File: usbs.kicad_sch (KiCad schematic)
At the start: 17 parts, among them J4 USB-A_Amphenol_UE27AC54100, J5 USB-C_GCT_USB4105-GF-A, J6 USB-C_GCT_USB4105-GF-A, U5 FT234XD-R

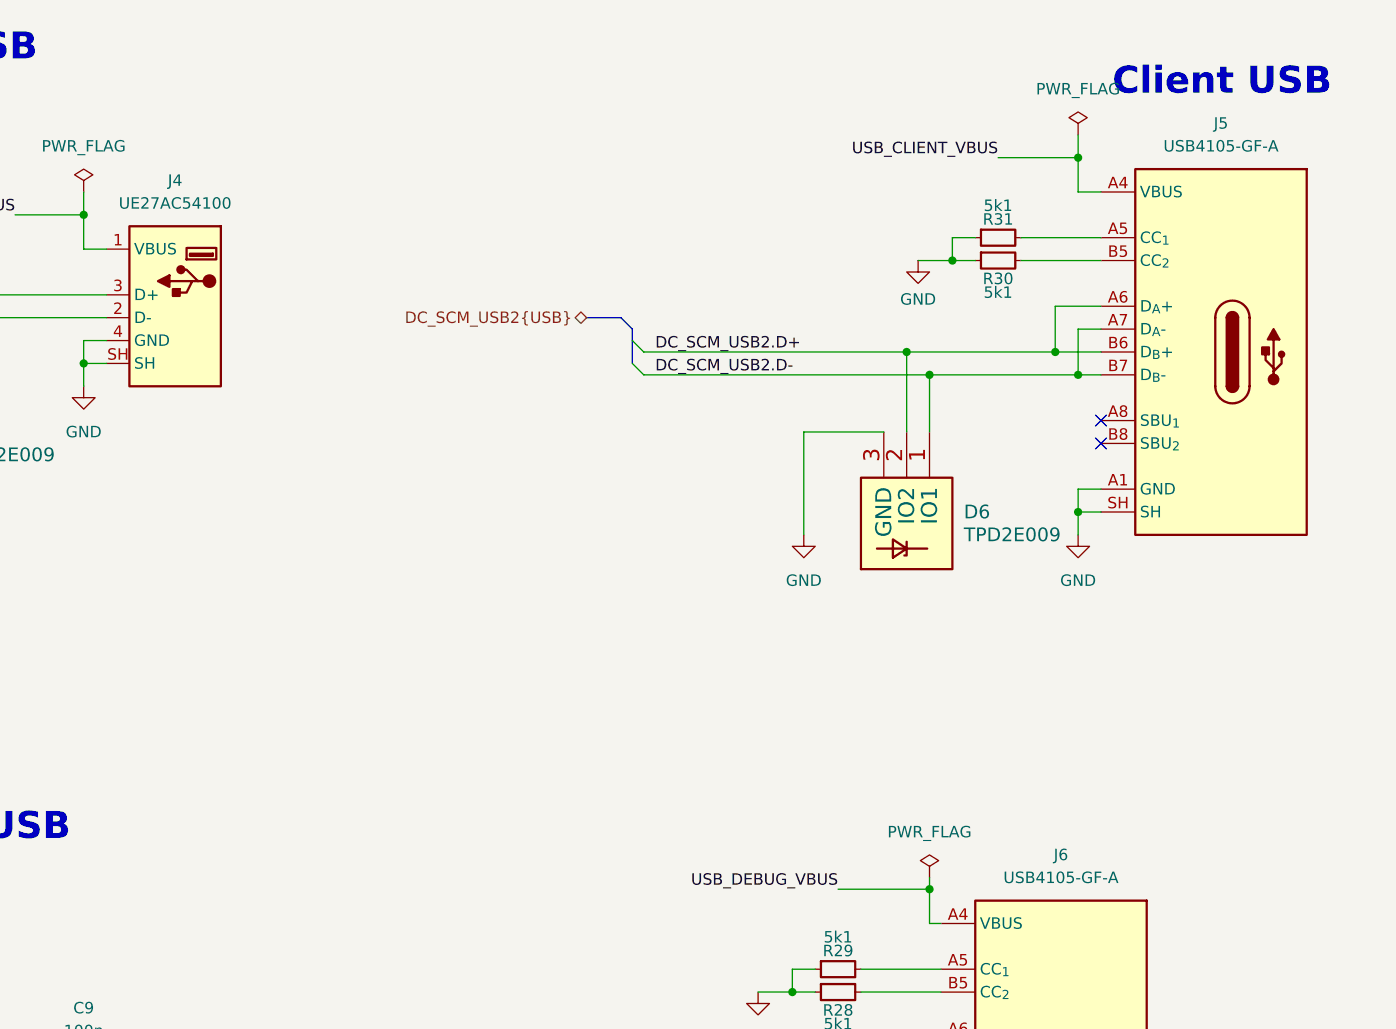
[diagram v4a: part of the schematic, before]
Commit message: [#92504] Update Annotation for connectors
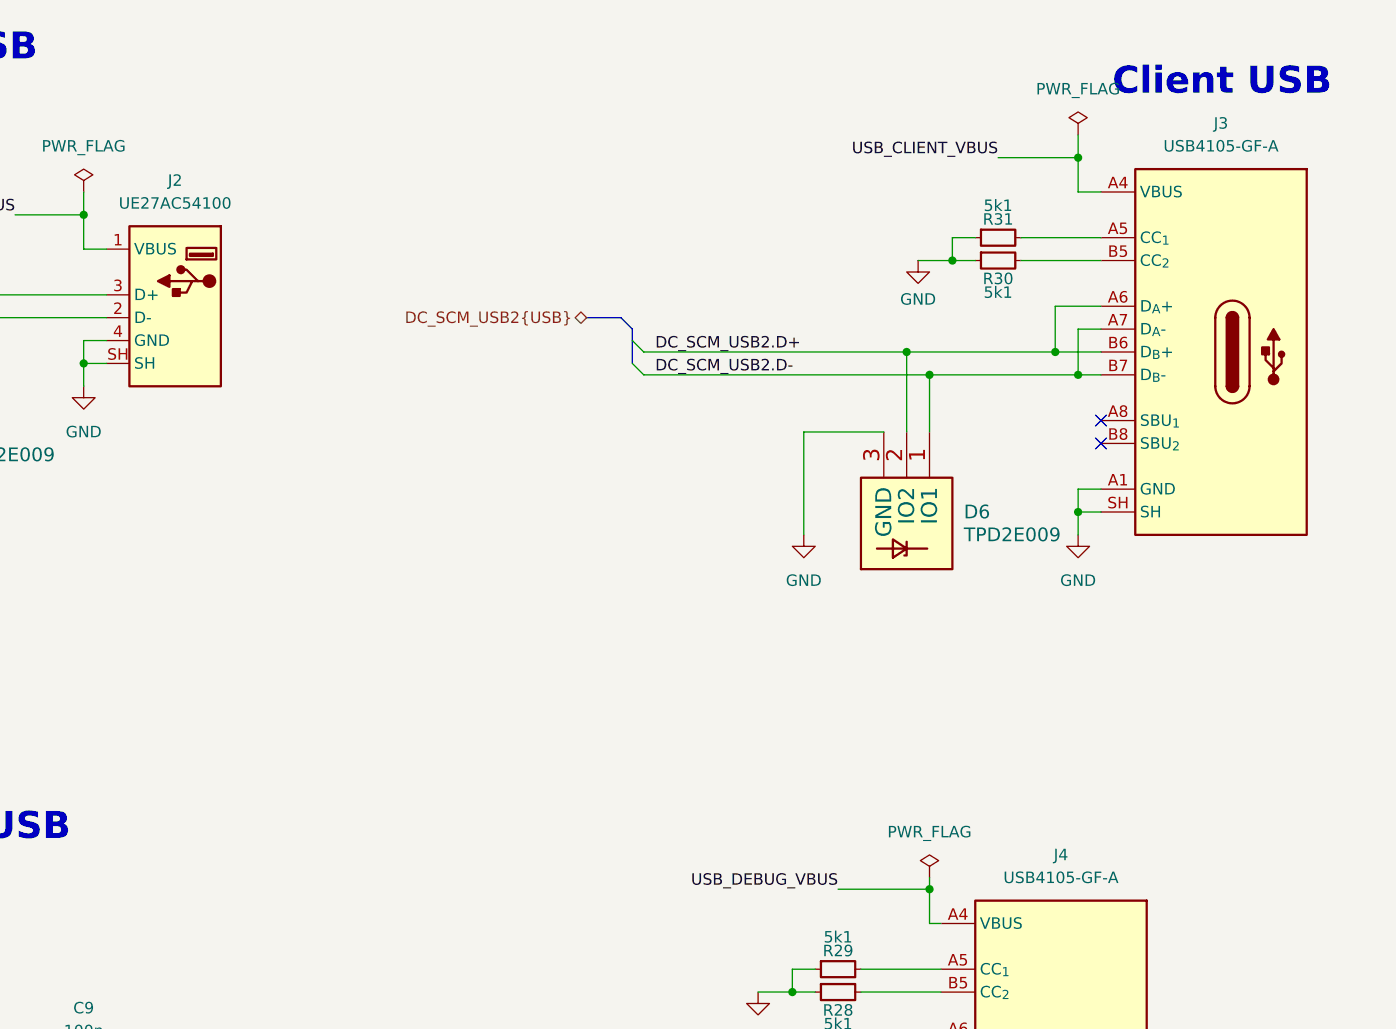
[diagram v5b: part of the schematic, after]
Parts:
- renumbered J4 to J2, J5 to J3, J6 to J4
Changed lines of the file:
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@@
 		(on_board yes)
 		(dnp no)
-		(property "Reference" "J5"
+		(property "Reference" "J3"
 			(at 208.915 33.02 0)
 			(effects
@@
 			(project ""
 				(path "/5d67ef28-5805-4f87-b722-2926dabf7f6e/07ab1158-ddfb-42f0-9fa7-f1beb51ab908"
-					(reference "J5")
+					(reference "J3")
 					(unit 1)
 				)
@@
 		(on_board yes)
 		(dnp no)
-		(property "Reference" "J6"
+		(property "Reference" "J4"
 			(at 191.135 114.3 0)
 			(effects
@@
 			(project "bmc-breakout-board"
 				(path "/5d67ef28-5805-4f87-b722-2926dabf7f6e/07ab1158-ddfb-42f0-9fa7-f1beb51ab908"
-					(reference "J6")
+					(reference "J4")
 					(unit 1)
 				)
@@
 		(on_board yes)
 		(dnp no)
-		(property "Reference" "J4"
+		(property "Reference" "J2"
 			(at 92.71 39.37 0)
 			(effects
@@
 			(project ""
 				(path "/5d67ef28-5805-4f87-b722-2926dabf7f6e/07ab1158-ddfb-42f0-9fa7-f1beb51ab908"
-					(reference "J4")
+					(reference "J2")
 					(unit 1)
 				)

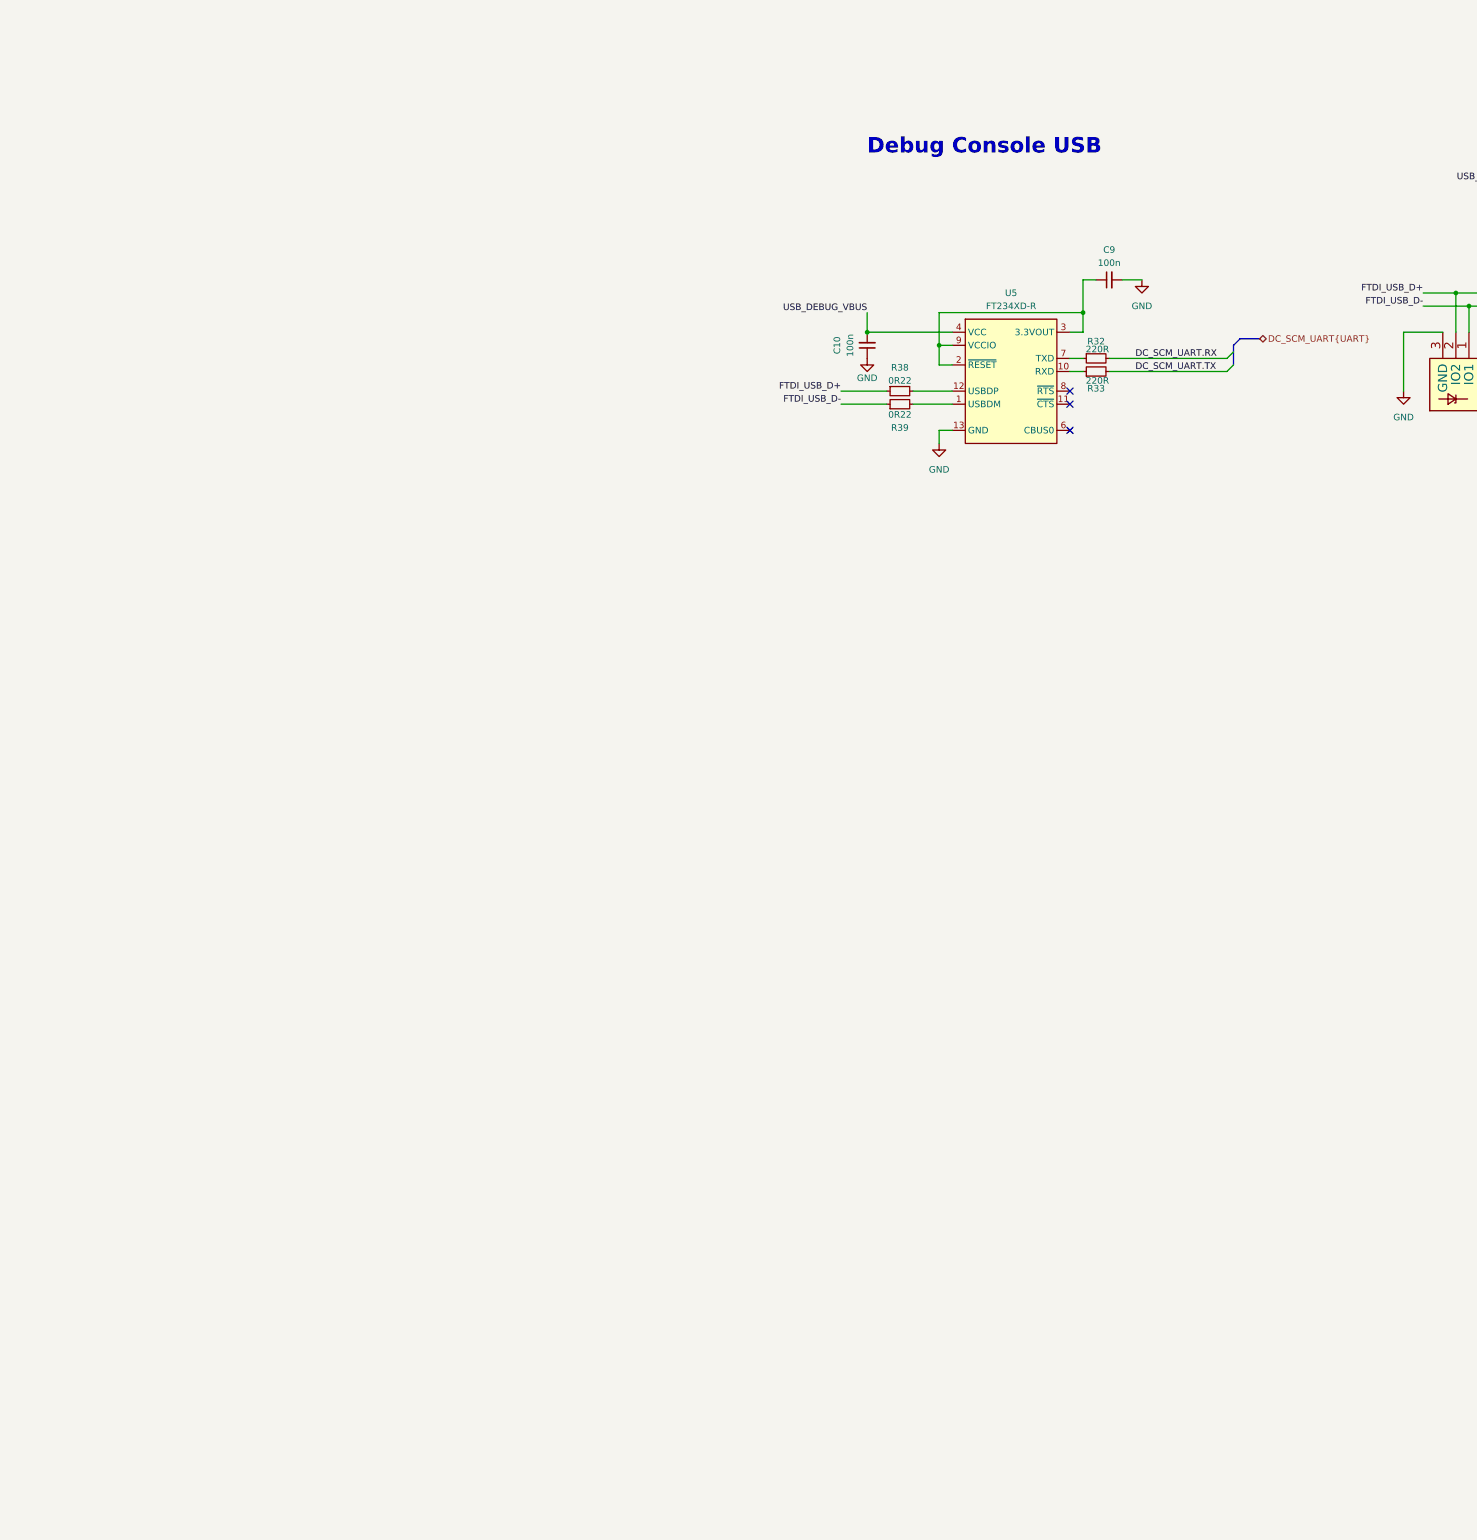
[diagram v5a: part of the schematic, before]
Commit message: [#92504] Align DC-SCM socket with connector
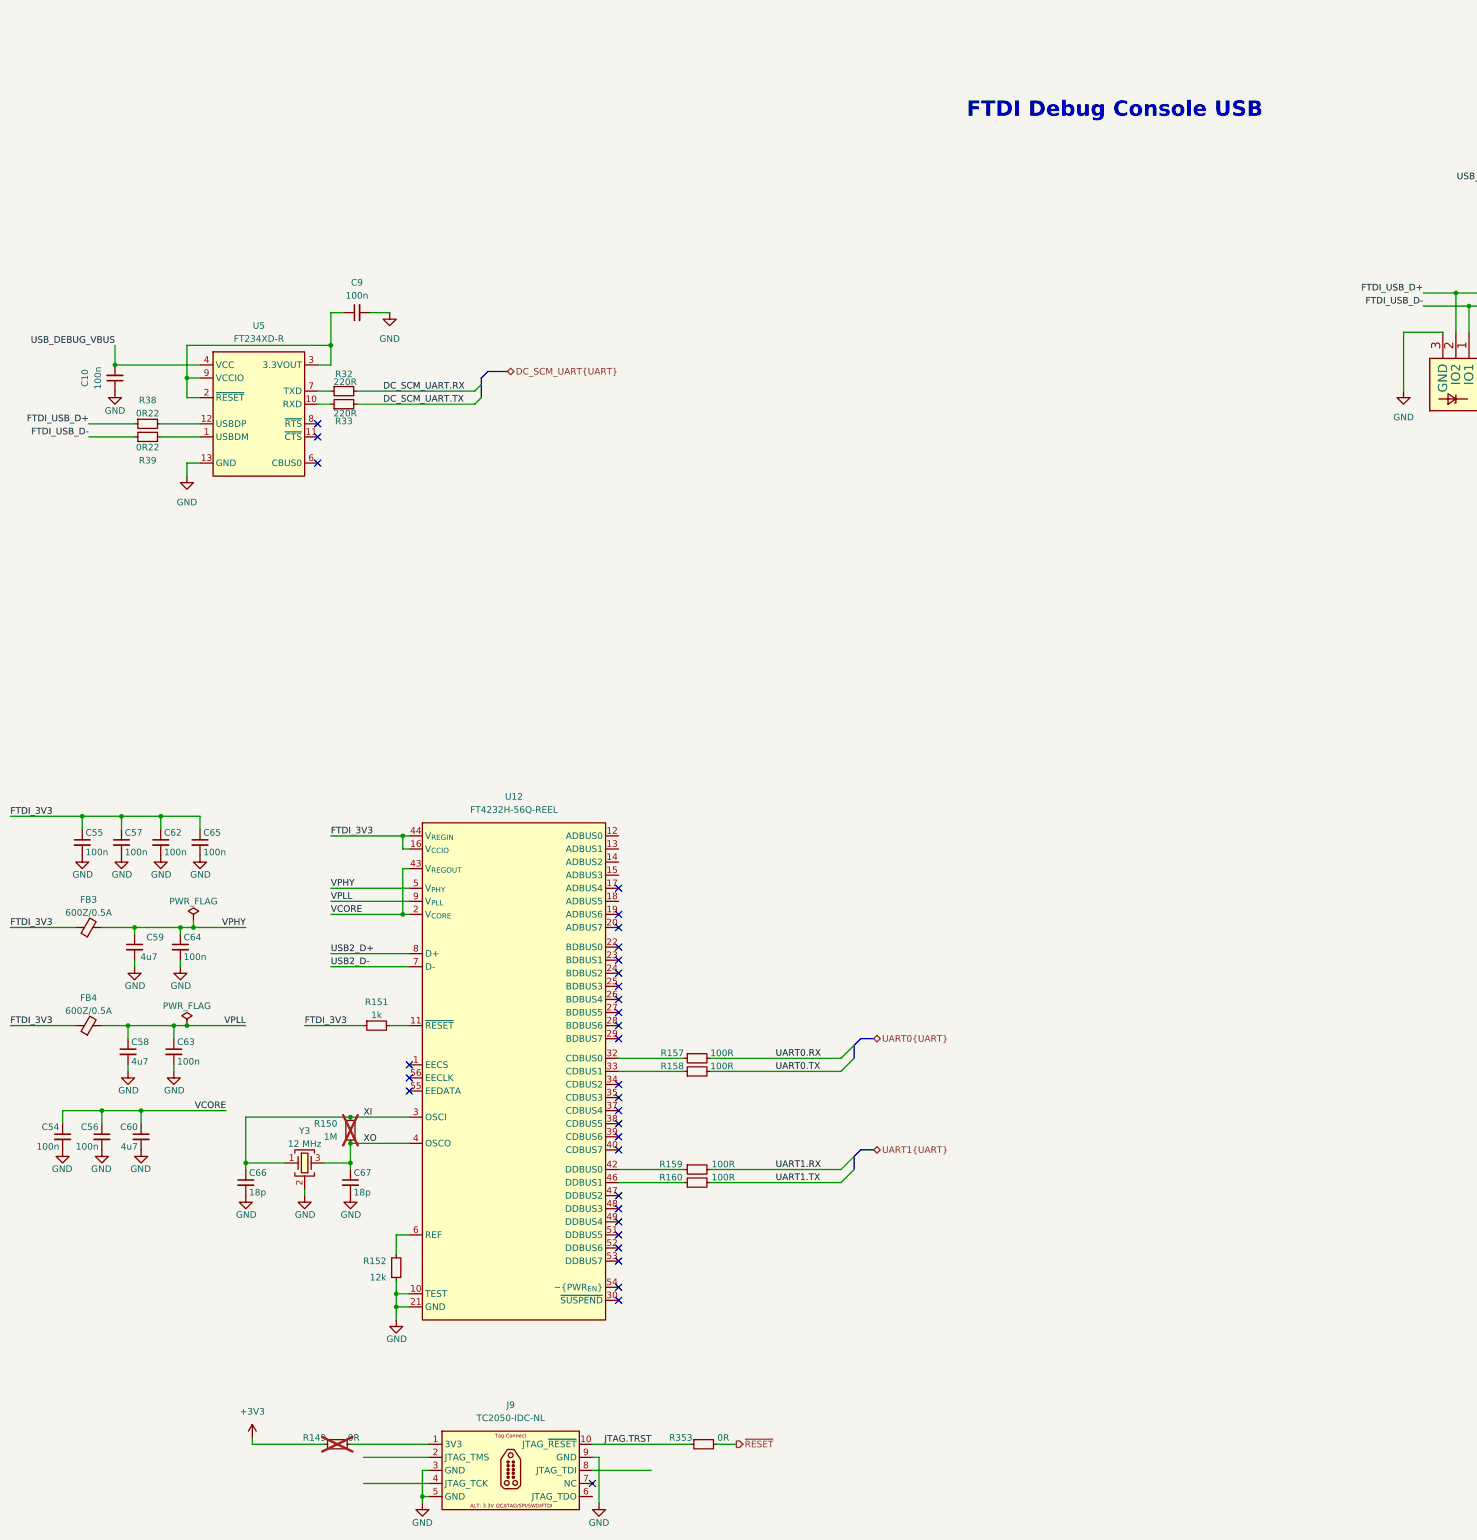
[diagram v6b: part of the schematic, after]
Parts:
- added C54, C55, C56, C57, C62, C63, C64, C65: C_100n_0402, antmicro-footprints:C_0402_1005Metric, symbol antmicroCapacitors0402:C_100n_0402
- added C58, C59, C60: C_4u7_0402, antmicro-footprints:C_0402_1005Metric, symbol antmicroCapacitors0402:C_4u7_0402
- added C66, C67: C_18p_0402, antmicro-footprints:C_0402_1005Metric, symbol antmicroCapacitors0402:C_18p_0402
- added FB3, FB4: FB_600Z_0.5A_Murata-BLM18AG_0603, antmicro-footprints:FB_0603_1608Metric, symbol antmicroFerriteBeadsandChips:FB_600Z_0.5A_Murata-BLM18AG_0603
- added J9: Tag-Connect_TC2050-IDC-NL_2x5_P1.27mm, antmicro-footprints:Tag-Connect_TC2050-IDC-NL_2x5_P1.27mm, symbol antmicroTestPoints:Tag-Connect_TC2050-IDC-NL_2x5_P1.27mm
- added R149, R353: R_0R_0402, antmicro-footprints:R_0402_1005Metric, symbol antmicroResistors0402:R_0R_0402
- added R150: R_1M_0402, antmicro-footprints:R_0402_1005Metric, symbol antmicroResistors0402:R_1M_0402
- added R151: R_1k_0402, antmicro-footprints:R_0402_1005Metric, symbol antmicroResistors0402:R_1k_0402
- added R152: R_12k_0402, antmicro-footprints:R_0402_1005Metric, symbol antmicroResistors0402:R_12k_0402
- added R157, R158, R159, R160: R_100R_0402, antmicro-footprints:R_0402_1005Metric, symbol antmicroResistors0402:R_100R_0402
- added U12: FT4232H_VQFN, antmicro-footprints:QFN-56-1EP_8x8mm_P0.5mm, symbol antmicroInterfaceControllers:FT4232H_VQFN
- added Y3: Resonator_12MHz_ABM8G, antmicro-footprints:Resonator_SMD_Abracon_ABM8G_3.2x2.5mm, symbol antmicroResonators:Resonator_12MHz_ABM8G
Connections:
- net GND: now also C54.2, C55.2, C56.2, C57.2, C58.2, C59.2, C60.2, C62.2, C63.2, C64.2, C65.2, C66.2, C67.2, J9.3, J9.5, J9.9, R152.1, U12.10 (TEST), U12.21 (GND), U12.41 (GND), U12.45 (GND), U12.57 (GND), Y3.2 (SH), Y3.4 (SH)
- new net: R158.1, U12.33 (CDBUS1)
- new net: J9.1, R149.2
- new net: R151.2, U12.11 (~{RESET})
- new net: R157.1, U12.32 (CDBUS0)
- new net: R159.1, U12.42 (DDBUS0)
- new net: R160.1, U12.46 (DDBUS1)
- new net: R152.2, U12.6 (REF)
- new net +3V3: R149.1
- new net FTDI_3V3: C55.1, C57.1, C62.1, C65.1, FB3.1, FB4.1, R151.1, U12.16 (V_{CCIO}), U12.36 (V_{CCIO}), U12.44 (V_{REGIN}), U12.50 (V_{CCIO})
- new net JTAG.TRST: J9.10, R353.1
- new net UART0.RX: R157.2
- new net UART0.TX: R158.2
- new net UART1.RX: R159.2
- new net UART1.TX: R160.2
- new net USB2_D+: U12.8 (D+)
- new net USB2_D-: U12.7 (D-)
- new net VCORE: C54.1, C56.1, C60.1, U12.2 (V_{CORE}), U12.31 (V_{CORE}), U12.43 (V_{REGOUT})
- new net VPHY: C59.1, C64.1, FB3.2, U12.5 (V_{PHY})
- new net VPLL: C58.1, C63.1, FB4.2, U12.9 (V_{PLL})
- new net XI: C66.1, R150.1, U12.3 (OSCI), Y3.1
- new net XO: C67.1, R150.2, U12.4 (OSCO), Y3.3
- new net ~{RESET}: R353.2
- no-connect marks 7 -> 36
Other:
- note added: "FTDI Debug Console USB"
- note removed: "Debug Console USB"
- moved on the sheet: C10, C9, R32, R33, R38, R39, U5

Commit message: [#92504] Connect FT4232H
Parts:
- removed C10, C9: C_100n_16V_X7R_0402, antmicro-footprints:C_0402_1005Metric, symbol antmicroCapacitors0402:C_100n_16V_X7R_0402
- removed C54, C55, C56, C57, C62, C63, C64, C65: C_100n_0402, antmicro-footprints:C_0402_1005Metric, symbol antmicroCapacitors0402:C_100n_0402
- removed C58, C59, C60: C_4u7_0402, antmicro-footprints:C_0402_1005Metric, symbol antmicroCapacitors0402:C_4u7_0402
- removed C66, C67: C_18p_0402, antmicro-footprints:C_0402_1005Metric, symbol antmicroCapacitors0402:C_18p_0402
- removed FB3, FB4: FB_600Z_0.5A_Murata-BLM18AG_0603, antmicro-footprints:FB_0603_1608Metric, symbol antmicroFerriteBeadsandChips:FB_600Z_0.5A_Murata-BLM18AG_0603
- removed J9: Tag-Connect_TC2050-IDC-NL_2x5_P1.27mm, antmicro-footprints:Tag-Connect_TC2050-IDC-NL_2x5_P1.27mm, symbol antmicroTestPoints:Tag-Connect_TC2050-IDC-NL_2x5_P1.27mm
- removed R149, R353: R_0R_0402, antmicro-footprints:R_0402_1005Metric, symbol antmicroResistors0402:R_0R_0402
- removed R150: R_1M_0402, antmicro-footprints:R_0402_1005Metric, symbol antmicroResistors0402:R_1M_0402
- removed R151: R_1k_0402, antmicro-footprints:R_0402_1005Metric, symbol antmicroResistors0402:R_1k_0402
- removed R152: R_12k_0402, antmicro-footprints:R_0402_1005Metric, symbol antmicroResistors0402:R_12k_0402
- removed R157, R158, R159, R160: R_100R_0402, antmicro-footprints:R_0402_1005Metric, symbol antmicroResistors0402:R_100R_0402
- removed U5: FT234XD-R, antmicro-footprints:DFN-12-1EP_3x3mm, symbol antmicroInterfaceControllers:FT234XD-R
- removed Y3: Resonator_12MHz_ABM8G, antmicro-footprints:Resonator_SMD_Abracon_ABM8G_3.2x2.5mm, symbol antmicroResonators:Resonator_12MHz_ABM8G
- added C14, C15, C16, C17, C18, C19, C20, C21: C_100n_16V_X7R_0402, antmicro-footprints:C_0402_1005Metric, symbol antmicroCapacitors0402:C_100n_16V_X7R_0402
- added C22, C23, C24: C_4u7_0402, antmicro-footprints:C_0402_1005Metric, symbol antmicroCapacitors0402:C_4u7_0402
- added C25, C26: C_18p_0402, antmicro-footprints:C_0402_1005Metric, symbol antmicroCapacitors0402:C_18p_0402
- added FB1, FB2: FB_600Z_0.5A_Murata-BLM18AG_0603, antmicro-footprints:FB_0603_1608Metric, symbol antmicroFerriteBeadsandChips:FB_600Z_0.5A_Murata-BLM18AG_0603
- added R26: R_12k_0402, antmicro-footprints:R_0402_1005Metric, symbol antmicroResistors0402:R_12k_0402
- added R34: R_1k_0402, antmicro-footprints:R_0402_1005Metric, symbol antmicroResistors0402:R_1k_0402
- added R40: R_1M_0402, antmicro-footprints:R_0402_1005Metric, symbol antmicroResistors0402:R_1M_0402
- added Y1: Resonator_12MHz_ABM8G, antmicro-footprints:Resonator_SMD_Abracon_ABM8G_3.2x2.5mm, symbol antmicroResonators:Resonator_12MHz_ABM8G
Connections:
- net FTDI_3V3 is gone; now on net +3V3: U12.16 (V_{CCIO}), U12.36 (V_{CCIO}), U12.44 (V_{REGIN}), U12.50 (V_{CCIO})
- net USB2_D+ is gone; now on an unnamed net: U12.8 (D+)
- net USB2_D- is gone; now on an unnamed net: U12.7 (D-)
- net +3V3: now also C14.1, C15.1, C16.1, C17.1, FB1.1, FB2.1, R34.1
- net GND: now also C14.2, C15.2, C16.2, C17.2, C18.2, C19.2, C20.2, C21.2, C22.1, C23.1, C24.1, C25.1, C26.1, R26.1, Y1.2 (SH), Y1.4 (SH)
- net VCORE: now also C20.1, C21.1, C24.2
- net VPHY: now also C18.1, C22.2, FB1.2
- net VPLL: now also C19.1, C23.2, FB2.2
- net XI: now also C25.2, R40.2, Y1.1
- net XO: now also C26.2, R40.1, Y1.3
- net at U12.33 (CDBUS1): now also R33.1
- net at R32.1: now also U12.32 (CDBUS0)
- net at U12.11 (~{RESET}): now also R34.2
- net at U12.6 (REF): now also R26.2
- no-connect marks 36 -> 31
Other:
- moved on the sheet: D9, J4, R28, R29, R32, R33, R38, R39, U12
